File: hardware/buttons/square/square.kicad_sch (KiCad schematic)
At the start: 10 parts

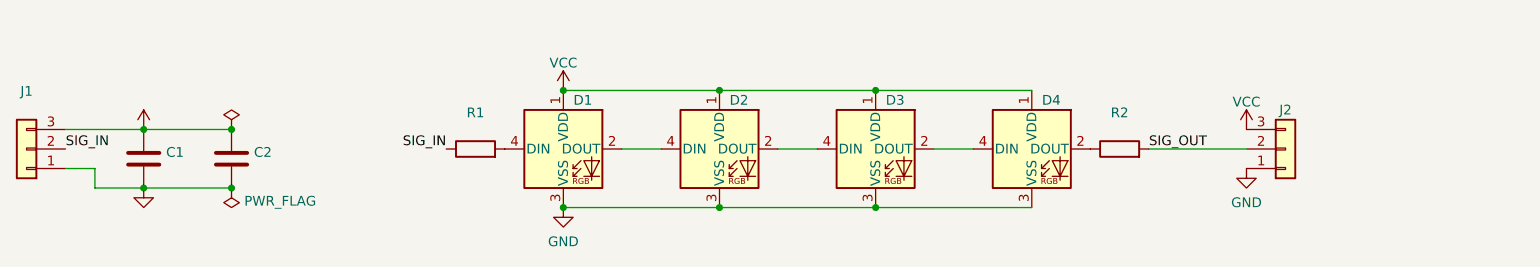
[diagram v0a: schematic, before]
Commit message: Add mounting holes
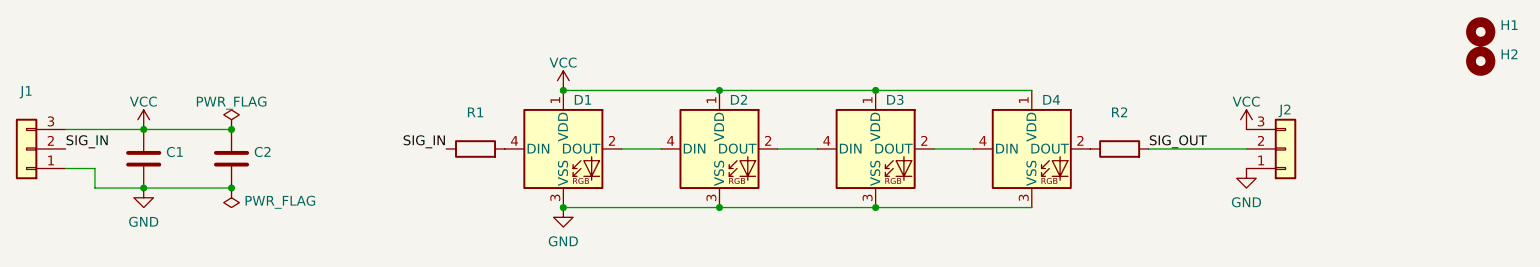
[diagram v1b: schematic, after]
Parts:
- added H1, H2: (no value), symbol Mechanical:MountingHole
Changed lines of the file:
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@@
       (effects (font (size 1.27 1.27)) hide)
     )
-    (property "Value" "" (id 1) (at 38.1 35.7942 0))
+    (property "Value" "VCC" (id 1) (at 38.1 35.7942 0))
     (property "Footprint" "" (id 2) (at 38.1 39.37 0)
       (effects (font (size 1.27 1.27)) hide)
@@
       (effects (font (size 1.27 1.27)) hide)
     )
-    (property "Value" "" (id 1) (at 49.53 35.7942 0))
+    (property "Value" "PWR_FLAG" (id 1) (at 49.53 35.7942 0))
     (property "Footprint" "" (id 2) (at 49.53 39.37 0)
       (effects (font (size 1.27 1.27)) hide)
@@
     (pin "2")
   )
+  (symbol (lib_id "Mechanical:MountingHole") (at 212.09 30.48 0) (unit 1)
+    (in_bom yes) (on_board yes) (fields_autoplaced)
+    (property "Reference" "H2" (id 0) (at 214.63 29.6453 0)
+      (effects (font (size 1.27 1.27)) (justify left))
+    )
+    (property "Value" "" (id 1) (at 214.63 32.1822 0)
+      (effects (font (size 1.27 1.27)) (justify left))
+    )
+    (property "Footprint" "" (id 2) (at 212.09 30.48 0)
+      (effects (font (size 1.27 1.27)) hide)
+    )
+    (property "Datasheet" "~" (id 3) (at 212.09 30.48 0)
+      (effects (font (size 1.27 1.27)) hide)
+    )
+  )
+  (symbol (lib_id "Mechanical:MountingHole") (at 212.09 26.67 0) (unit 1)
+    (in_bom yes) (on_board yes) (fields_autoplaced)
+    (property "Reference" "H1" (id 0) (at 214.63 25.8353 0)
+      (effects (font (size 1.27 1.27)) (justify left))
+    )
+    (property "Value" "" (id 1) (at 214.63 28.3722 0)
+      (effects (font (size 1.27 1.27)) (justify left))
+    )
+    (property "Footprint" "" (id 2) (at 212.09 26.67 0)
+      (effects (font (size 1.27 1.27)) hide)
+    )
+    (property "Datasheet" "~" (id 3) (at 212.09 26.67 0)
+      (effects (font (size 1.27 1.27)) hide)
+    )
+  )
   (symbol (lib_id "Connector_Generic:Conn_01x03") (at 186.69 41.91 0) (mirror x) (unit 1)
     (in_bom yes) (on_board yes)
@@
       (effects (font (size 1.27 1.27)) hide)
     )
-    (property "Value" "" (id 1) (at 38.1 51.4334 0))
+    (property "Value" "GND" (id 1) (at 38.1 51.4334 0))
     (property "Footprint" "" (id 2) (at 38.1 46.99 0)
       (effects (font (size 1.27 1.27)) hide)
@@
       (reference "D4") (unit 1) (value "WS2812B") (footprint "LED_SMD:LED_WS2812B_PLCC4_5.0x5.0mm_P3.2mm")
     )
+    (path "/7da9bb3f-a519-4511-84d8-bfc422090ff1"
+      (reference "H1") (unit 1) (value "MountingHole") (footprint "MountingHole:MountingHole_3.2mm_M3")
+    )
+    (path "/6b2799e6-ae08-4388-a66e-4e700572d773"
+      (reference "H2") (unit 1) (value "MountingHole") (footprint "MountingHole:MountingHole_3.2mm_M3")
+    )
     (path "/e8312cc4-6502-4783-b578-55c01e0393af"
